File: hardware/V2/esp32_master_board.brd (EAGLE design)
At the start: 65 x 35 mm, 66 parts, among them IC1 SN74HC138PW, IC2 MAX17502EATB+T, IC3 WS2812B, IC4 WS2812B, SW1 B3U-1000P-2P-SMD

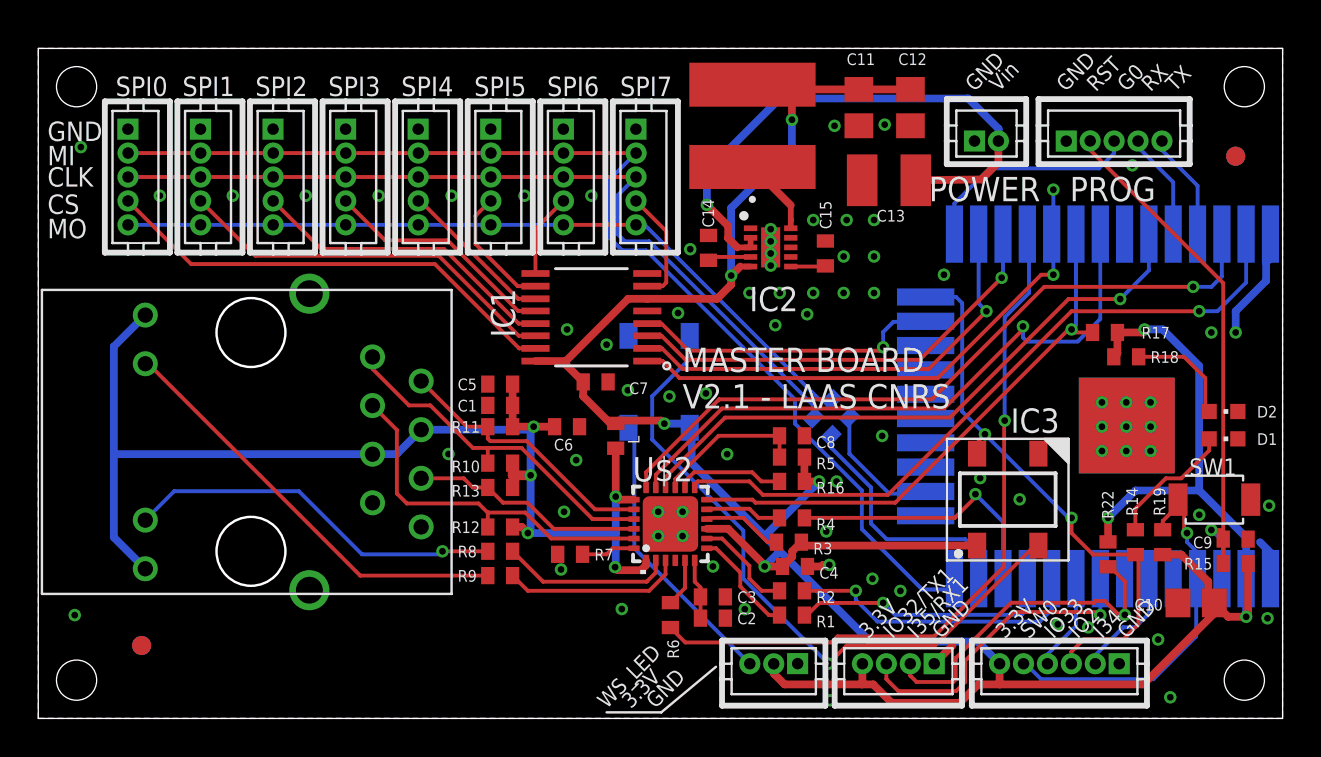
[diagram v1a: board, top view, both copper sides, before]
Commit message: Fix 0402 footprint to comply with seeed, fix HR911105A footprint, add labels for L1,U,U,U,U, update board revision to V2.2
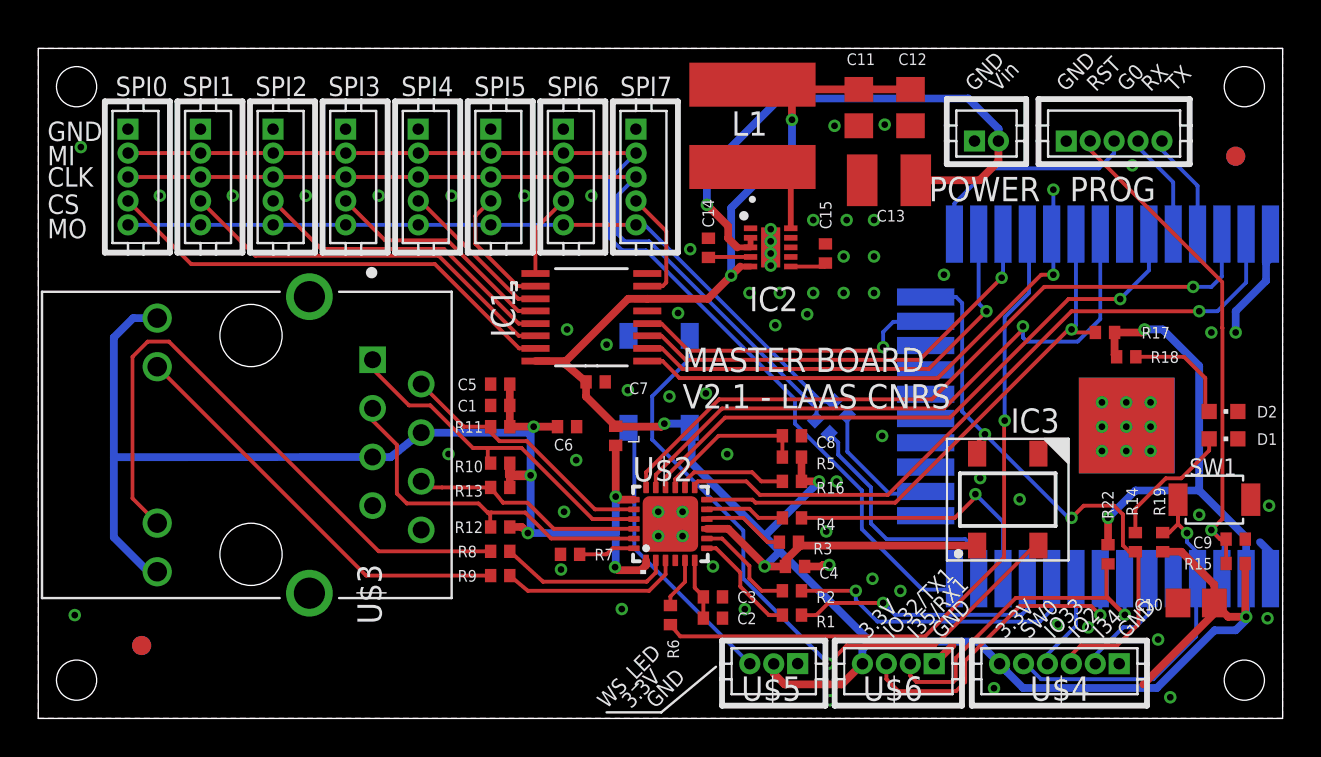
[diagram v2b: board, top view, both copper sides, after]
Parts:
- C1, C14, C15, C2, C3, C4, C5, C6, C7, C8, C9: device resistor:C0402 -> resistor:0402
- L, R1, R10, R11, R12, R13, R14, R15, R16, R17, R18, R19, R2, R20, R21, R22, R3, R4, R5, R6, R7, R8, R9: device resistor:R0402 -> resistor:0402
- U$3: device HR911105A:RJ45 -> HR911105A_bis:HANRUN_HR911105A
- moved U$3 0.57 mm to (11.1, 14.3), turned to 90 degrees
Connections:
- net GND: now also U$3.15, U$3.16, U$3.8; no longer U$3.GND, U$3.SHIELD1, U$3.SHIELD2
- net N$10: now also U$3.6; no longer U$3.RD-
- net N$11: now also U$3.11; no longer U$3.Y-
- net N$12: now also U$3.10; no longer U$3.G-
- net N$7: now also U$3.1; no longer U$3.TD+
- net N$8: now also U$3.2; no longer U$3.TD-
- net N$9: now also U$3.3; no longer U$3.RD+
- net VDD: now also U$3.12, U$3.4, U$3.5, U$3.9; no longer U$3.G+, U$3.P4, U$3.P5, U$3.Y+
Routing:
- net N$11: track 19.9 -> 32.8 mm, vias 1 -> 0
- net VDD: track 64.9 -> 67.1 mm
- net RST: track 30.2 -> 28.5 mm
- net N$18: track 4.03 -> 5.15 mm
- net IO2: track 29.9 -> 30.9 mm
- net N$12: track 22.5 -> 21.9 mm
- net GND: track 21.4 -> 21.5 mm, vias 75 -> 76
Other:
- board text added: "MASTER BOARD V2.2 - LAAS CNRS"
